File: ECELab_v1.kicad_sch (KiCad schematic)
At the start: 0 parts

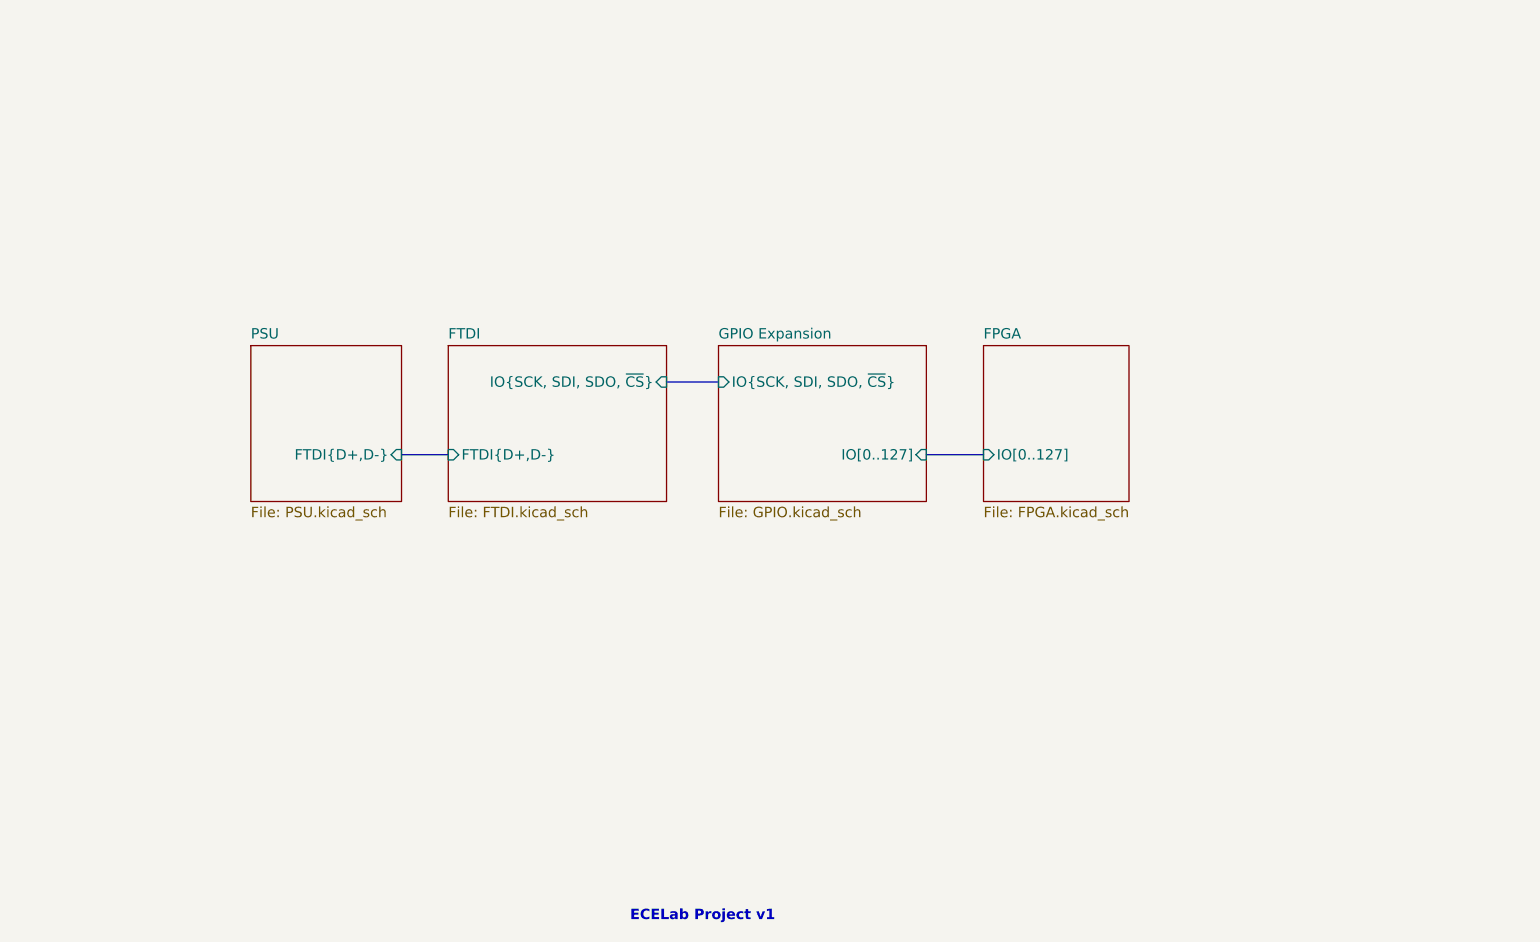
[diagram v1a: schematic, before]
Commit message: Complete SPI Design
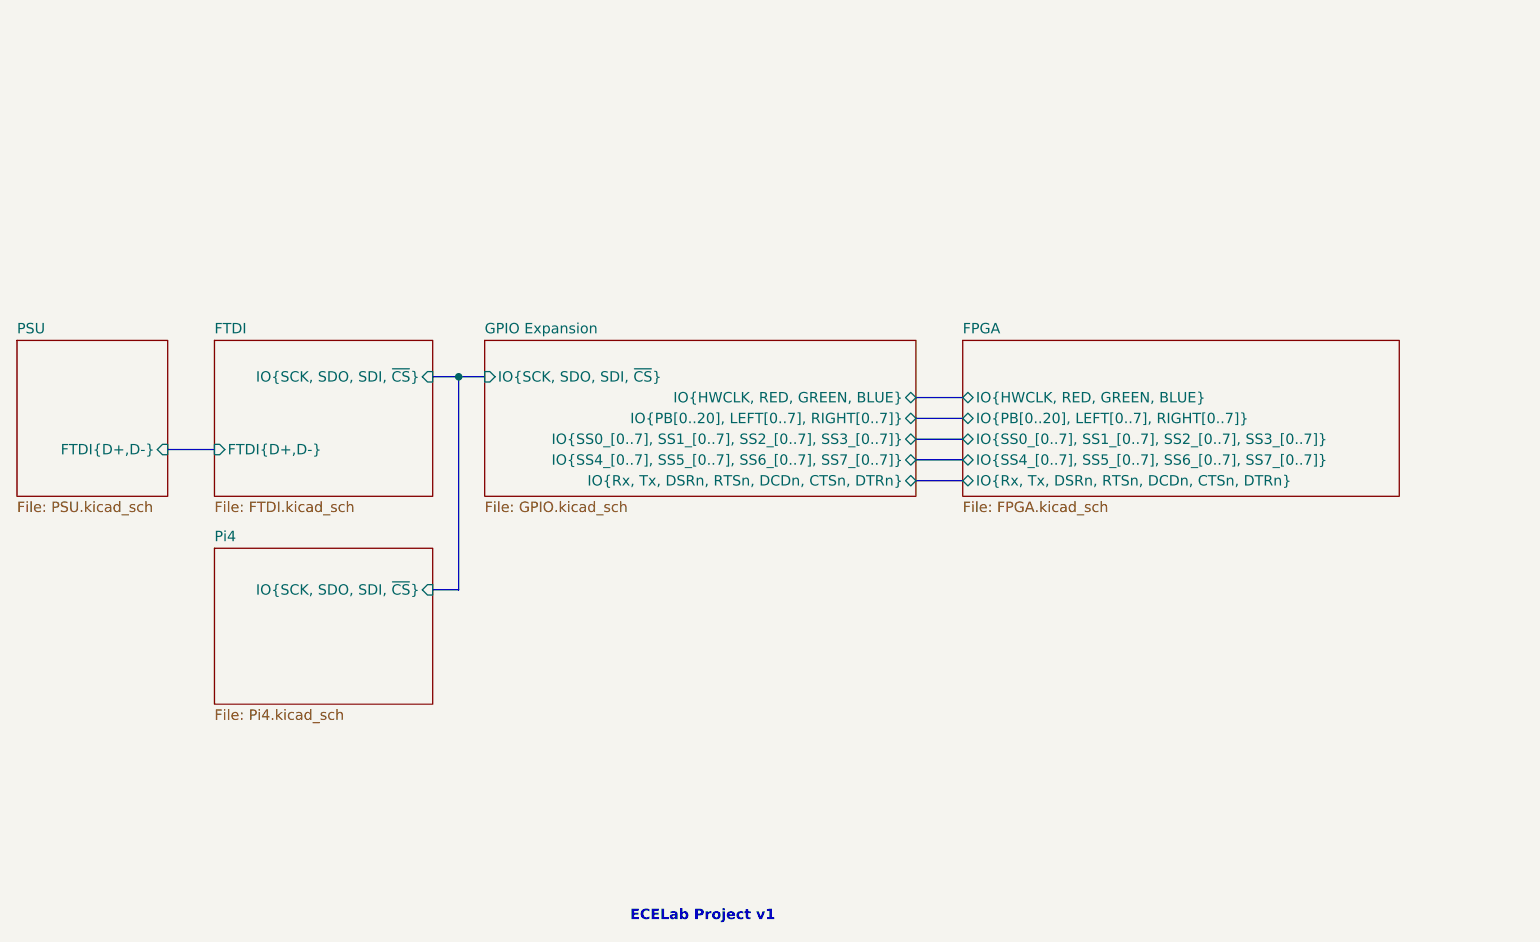
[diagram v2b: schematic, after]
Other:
- added sheet Pi4 (Pi4.kicad_sch)
- sheet FPGA ports: added IO{HWCLK, RED, GREEN, BLUE}, IO{PB[0..20], LEFT[0..7], RIGHT[0..7]}, IO{Rx, Tx, DSRn, RTSn, DCDn, CTSn, DTRn}, IO{SS0_[0..7], SS1_[0..7], SS2_[0..7], SS3_[0..7]}, IO{SS4_[0..7], SS5_[0..7], SS6_[0..7], SS7_[0..7]}; removed IO[0..127]
- sheet FTDI ports: added IO{SCK, SDO, SDI, ~{CS}}; removed IO{SCK, SDI, SDO, ~{CS}}
- sheet GPIO Expansion ports: added IO{HWCLK, RED, GREEN, BLUE}, IO{PB[0..20], LEFT[0..7], RIGHT[0..7]}, IO{Rx, Tx, DSRn, RTSn, DCDn, CTSn, DTRn}, IO{SCK, SDO, SDI, ~{CS}}, IO{SS0_[0..7], SS1_[0..7], SS2_[0..7], SS3_[0..7]}, IO{SS4_[0..7], SS5_[0..7], SS6_[0..7], SS7_[0..7]}; removed IO[0..127], IO{SCK, SDI, SDO, ~{CS}}

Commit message: Update 1
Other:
- sheet FPGA ports: added IO{IO0, IO1, IO2, IO3}; removed none
- sheet FTDI ports: added IO{SCK, SDA}; removed IO{SCK, SDO, SDI, ~{CS}}
- sheet GPIO Expansion ports: added IO{SCK, SDA}; removed IO{SCK, SDO, SDI, ~{CS}}
- sheet Pi4 ports: added IO{IO0, IO1, IO2, IO3}, IO{SCK, SDA}; removed IO{SCK, SDO, SDI, ~{CS}}

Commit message: Update 2nd iteration
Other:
- added sheet FTDI - GPIO Stream (FTDI-GPIO.kicad_sch)
- sheet FPGA ports: added none; removed IO{IO0, IO1, IO2, IO3}
- sheet FTDI ports: added IO{SCK[0..1], SDA[0..1]}; removed IO{SCK, SDA}
- sheet GPIO Expansion ports: added IO{SCK[0..1], SDA[0..1]}, IO{SS6_[0..7], SS7_[0..7]}, MCP5{SEL, PWR}, MCP5{SEL, PWR}, {INTA.MCP[0..7], INTB.MCP[0..7]}; removed IO{SCK, SDA}
- sheet Pi4 ports: added IO{SCK[0..1], SDA[0..1]}, {INTA.MCP[0..7], INTB.MCP[0..7]}; removed IO{IO0, IO1, IO2, IO3}, IO{SCK, SDA}

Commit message: Update 7/30
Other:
- sheet FTDI - GPIO Stream ports: added IO{LEFT[0..7], RIGHT[0..7]}; removed MCP5{SEL, PWR}
- sheet GPIO Expansion ports: added IO{LEFT[0..7], RIGHT[0..7]}, IO{SS6_[0..7], SS7_[0..7}}, MCP6{SEL, PWR}; removed IO{SS6_[0..7], SS7_[0..7]}, MCP5{SEL, PWR}
- sheet Pi4 ports: added MCP5{SEL, PWR}, MCP6{SEL, PWR}; removed none
